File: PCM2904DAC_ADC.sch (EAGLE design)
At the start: 48 parts, among them IC1 LM358D, Q1 12MHz, X1 V+, D-, D+, GND, X2 1503_09, X3 1503_09

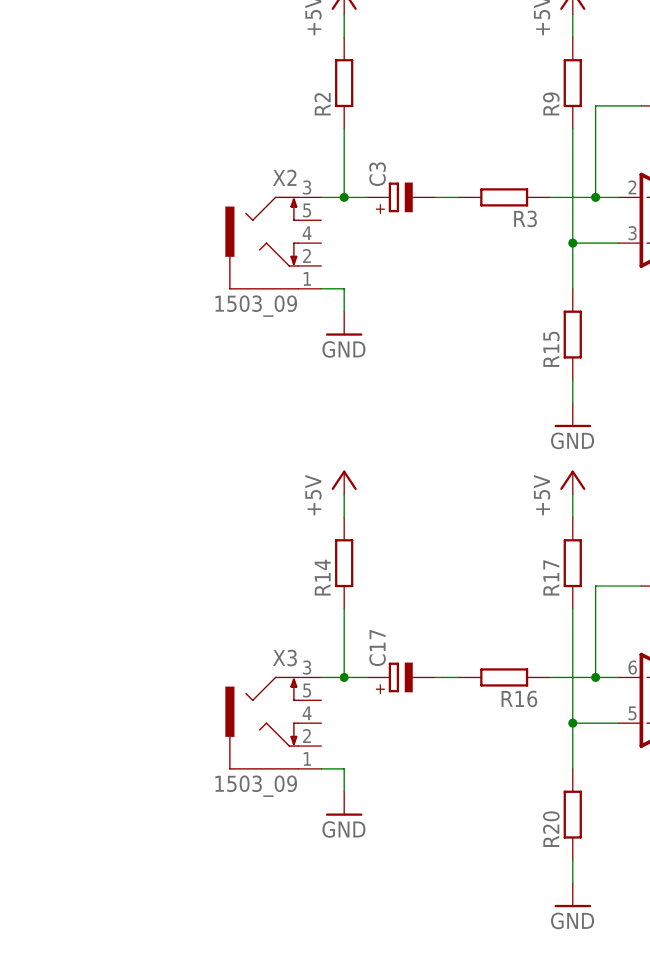
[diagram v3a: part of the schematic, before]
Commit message: cambiado tamaño del led, fichas stereo, y otras cosas sueltas
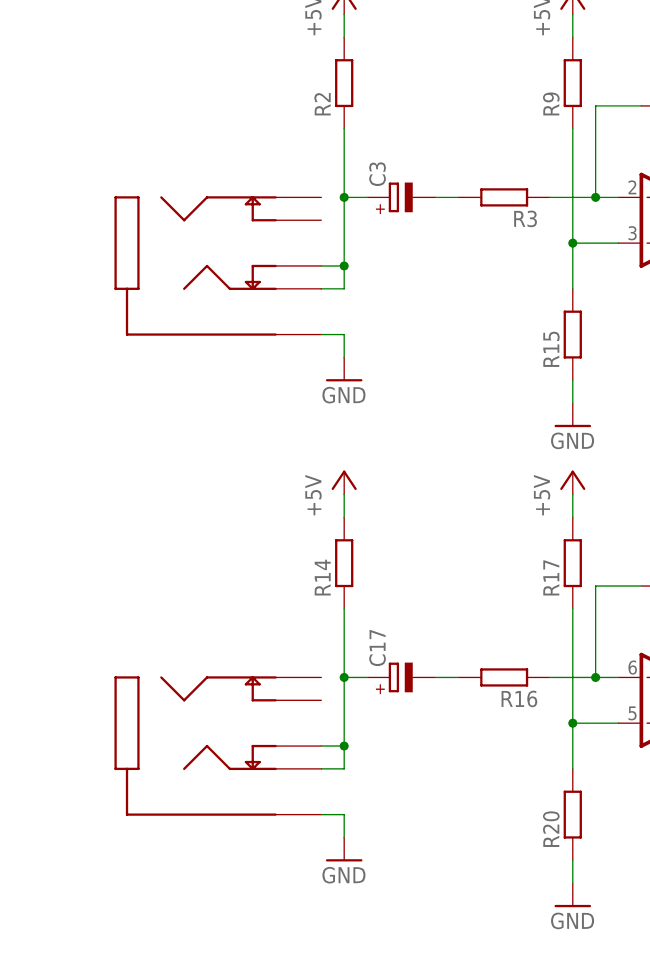
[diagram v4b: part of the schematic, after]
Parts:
- removed X2, X3: 1503_09, con-lumberg:1503_09
- added U$1, U$8: 1/8STEREO, bleep t2:1/8STEREO
- C4: device rcl:CPOL-EU153CLV-0505 -> rcl:CPOL-EU153CLV-0807
- LED1: device led:LEDSML1206 -> led:LEDCHIPLED_0805
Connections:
- net GND: now also U$1.P$1, U$8.P$1; no longer X2.1, X3.1
- net N$5: now also U$8.P$4, U$8.P$5; no longer X2.3
- net N$7: now also U$1.P$4, U$1.P$5; no longer X3.3
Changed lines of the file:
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@@
 <part name="X1" library="con-berg" deviceset="PN61729" device="" value="V+, D-, D+, GND"/>
 <part name="GND2" library="supply1" deviceset="GND" device=""/>
-<part name="C4" library="rcl" deviceset="CPOL-EU" device="153CLV-0505" value="100u "/>
+<part name="C4" library="rcl" library_urn="urn:adsk.eagle:library:334" deviceset="CPOL-EU" device="153CLV-0807" package3d_urn="urn:adsk.eagle:package:23400/1" value="100u "/>
 <part name="R4" library="rcl" deviceset="R-EU_" device="R1206" value="22"/>
 <part name="R5" library="rcl" deviceset="R-EU_" device="R1206" value="22"/>
@@
 <part name="R8" library="rcl" deviceset="R-EU_" device="R1206" value="1k2"/>
 <part name="PCM2904" library="PCM2904" deviceset="PCM2904" device=""/>
-<part name="LED1" library="led" deviceset="LED" device="SML1206" value="2.65V, 2mA"/>
+<part name="LED1" library="led" library_urn="urn:adsk.eagle:library:259" deviceset="LED" device="CHIPLED_0805" package3d_urn="urn:adsk.eagle:package:15821/1" value="2.65V, 2mA"/>
 <part name="IC2" library="bt_regulator" deviceset="LM2931-ADJ" device="M"/>
 <part name="R12" library="rcl" deviceset="R-EU_" device="R1206" value="5k7"/>
 <part name="R13" library="rcl" deviceset="R-EU_" device="R1206" value="10k"/>
-<part name="X2" library="con-lumberg" library_urn="urn:adsk.eagle:library:163" deviceset="1503_09" device="" package3d_urn="urn:adsk.eagle:package:8555/1"/>
 <part name="IC1" library="linear" library_urn="urn:adsk.eagle:library:262" deviceset="LM358" device="D" package3d_urn="urn:adsk.eagle:package:16404/2"/>
 <part name="R2" library="rcl" library_urn="urn:adsk.eagle:library:334" deviceset="R-EU_" device="R1206W" package3d_urn="urn:adsk.eagle:package:23539/1"/>
@@
 <part name="P+6" library="supply1" library_urn="urn:adsk.eagle:library:371" deviceset="+5V" device=""/>
 <part name="C10" library="rcl" library_urn="urn:adsk.eagle:library:334" deviceset="CPOL-EU" device="153CLV-0505" package3d_urn="urn:adsk.eagle:package:23402/1" value="10u"/>
-<part name="X3" library="con-lumberg" library_urn="urn:adsk.eagle:library:163" deviceset="1503_09" device="" package3d_urn="urn:adsk.eagle:package:8555/1"/>
 <part name="R14" library="rcl" library_urn="urn:adsk.eagle:library:334" deviceset="R-EU_" device="R1206W" package3d_urn="urn:adsk.eagle:package:23539/1"/>
 <part name="R16" library="rcl" library_urn="urn:adsk.eagle:library:334" deviceset="R-EU_" device="R1206W" package3d_urn="urn:adsk.eagle:package:23539/1"/>
@@
 <part name="P+9" library="supply1" library_urn="urn:adsk.eagle:library:371" deviceset="+5V" device=""/>
 <part name="GND11" library="supply1" deviceset="GND" device=""/>
+<part name="U$8" library="bleep t2" deviceset="1/8STEREO" device=""/>
+<part name="U$1" library="bleep t2" deviceset="1/8STEREO" device=""/>
 </parts>
 <sheets>
@@
 <instance part="R12" gate="G$1" x="-35.56" y="40.64" rot="R90"/>
 <instance part="R13" gate="G$1" x="-35.56" y="27.94" rot="R270"/>
-<instance part="X2" gate="G$1" x="-86.36" y="-25.4" rot="MR0"/>
 <instance part="IC1" gate="A" x="-40.64" y="-22.86" rot="MR180"/>
 <instance part="R2" gate="G$1" x="-78.74" y="-7.62" rot="R90"/>
@@
 <instance part="P+2" gate="1" x="-78.74" y="2.54"/>
 <instance part="P+3" gate="1" x="-53.34" y="2.54"/>
-<instance part="GND5" gate="1" x="-78.74" y="-35.56"/>
+<instance part="GND5" gate="1" x="-78.74" y="-40.64"/>
 <instance part="GND6" gate="1" x="-53.34" y="-45.72"/>
 <instance part="P+4" gate="1" x="-86.36" y="50.8"/>
@@
 <instance part="P+6" gate="1" x="40.64" y="88.9"/>
 <instance part="C10" gate="G$1" x="-12.7" y="-76.2" rot="R90"/>
-<instance part="X3" gate="G$1" x="-86.36" y="-78.74" rot="MR0"/>
 <instance part="R14" gate="G$1" x="-78.74" y="-60.96" rot="R90"/>
 <instance part="R16" gate="G$1" x="-60.96" y="-73.66" rot="R180"/>
@@
 <instance part="P+7" gate="1" x="-78.74" y="-50.8"/>
 <instance part="P+8" gate="1" x="-53.34" y="-50.8"/>
-<instance part="GND9" gate="1" x="-78.74" y="-88.9"/>
+<instance part="GND9" gate="1" x="-78.74" y="-93.98"/>
 <instance part="GND10" gate="1" x="-53.34" y="-99.06"/>
 <instance part="IC1" gate="B" x="-40.64" y="-76.2" rot="MR180"/>
@@
 <instance part="P+9" gate="1" x="-12.7" y="-30.48"/>
 <instance part="GND11" gate="1" x="-12.7" y="-58.42"/>
+<instance part="U$8" gate="G$1" x="-104.14" y="-25.4" rot="MR180"/>
+<instance part="U$1" gate="G$1" x="-104.14" y="-78.74" rot="MR180"/>
 </instances>
 <busses>
@@
 </segment>
 <segment>
-<pinref part="GND5" gate="1" pin="GND"/>
-<wire x1="-78.74" y1="-33.02" x2="-78.74" y2="-30.48" width="0.1524" layer="91"/>
-<pinref part="X2" gate="G$1" pin="1"/>
-<wire x1="-78.74" y1="-30.48" x2="-81.28" y2="-30.48" width="0.1524" layer="91"/>
-</segment>
-<segment>
 <pinref part="GND6" gate="1" pin="GND"/>
 <pinref part="R15" gate="G$1" pin="1"/>
@@
 <pinref part="GND8" gate="1" pin="GND"/>
 <wire x1="63.5" y1="22.86" x2="63.5" y2="25.4" width="0.1524" layer="91"/>
-</segment>
-<segment>
-<pinref part="GND9" gate="1" pin="GND"/>
-<wire x1="-78.74" y1="-86.36" x2="-78.74" y2="-83.82" width="0.1524" layer="91"/>
-<pinref part="X3" gate="G$1" pin="1"/>
-<wire x1="-78.74" y1="-83.82" x2="-81.28" y2="-83.82" width="0.1524" layer="91"/>
 </segment>
 <segment>
@@
 <junction x="-7.62" y="-53.34"/>
 </segment>
+<segment>
+<pinref part="U$8" gate="G$1" pin="P$1"/>
+<pinref part="GND5" gate="1" pin="GND"/>
+<wire x1="-81.28" y1="-35.56" x2="-78.74" y2="-35.56" width="0.1524" layer="91"/>
+<wire x1="-78.74" y1="-35.56" x2="-78.74" y2="-38.1" width="0.1524" layer="91"/>
+</segment>
+<segment>
+<pinref part="U$1" gate="G$1" pin="P$1"/>
+<pinref part="GND9" gate="1" pin="GND"/>
+<wire x1="-81.28" y1="-88.9" x2="-78.74" y2="-88.9" width="0.1524" layer="91"/>
+<wire x1="-78.74" y1="-88.9" x2="-78.74" y2="-91.44" width="0.1524" layer="91"/>
+</segment>
 </net>
 <net name="N$4" class="0">
@@
 <net name="N$5" class="0">
 <segment>
-<pinref part="X2" gate="G$1" pin="3"/>
 <pinref part="R2" gate="G$1" pin="1"/>
-<wire x1="-81.28" y1="-20.32" x2="-78.74" y2="-20.32" width="0.1524" layer="91"/>
 <wire x1="-78.74" y1="-20.32" x2="-78.74" y2="-12.7" width="0.1524" layer="91"/>
 <pinref part="C3" gate="G$1" pin="+"/>
 <wire x1="-76.2" y1="-20.32" x2="-78.74" y2="-20.32" width="0.1524" layer="91"/>
 <junction x="-78.74" y="-20.32"/>
+<pinref part="U$8" gate="G$1" pin="P$5"/>
+<wire x1="-81.28" y1="-30.48" x2="-78.74" y2="-30.48" width="0.1524" layer="91"/>
+<wire x1="-78.74" y1="-30.48" x2="-78.74" y2="-27.94" width="0.1524" layer="91"/>
+<pinref part="U$8" gate="G$1" pin="P$4"/>
+<wire x1="-78.74" y1="-27.94" x2="-78.74" y2="-20.32" width="0.1524" layer="91"/>
+<wire x1="-81.28" y1="-27.94" x2="-78.74" y2="-27.94" width="0.1524" layer="91"/>
+<junction x="-78.74" y="-27.94"/>
 </segment>
 </net>
@@
 <net name="N$7" class="0">
 <segment>
-<pinref part="X3" gate="G$1" pin="3"/>
 <pinref part="R14" gate="G$1" pin="1"/>
-<wire x1="-81.28" y1="-73.66" x2="-78.74" y2="-73.66" width="0.1524" layer="91"/>
 <wire x1="-78.74" y1="-73.66" x2="-78.74" y2="-66.04" width="0.1524" layer="91"/>
 <pinref part="C17" gate="G$1" pin="+"/>
 <wire x1="-76.2" y1="-73.66" x2="-78.74" y2="-73.66" width="0.1524" layer="91"/>
 <junction x="-78.74" y="-73.66"/>
-</segment>
-</net>
+<pinref part="U$1" gate="G$1" pin="P$5"/>
+<wire x1="-81.28" y1="-83.82" x2="-78.74" y2="-83.82" width="0.1524" layer="91"/>
+<wire x1="-78.74" y1="-83.82" x2="-78.74" y2="-81.28" width="0.1524" layer="91"/>
+<pinref part="U$1" gate="G$1" pin="P$4"/>
+<wire x1="-78.74" y1="-81.28" x2="-78.74" y2="-73.66" width="0.1524" layer="91"/>
+<wire x1="-81.28" y1="-81.28" x2="-78.74" y2="-81.28" width="0.1524" layer="91"/>
+<junction x="-78.74" y="-81.28"/>
+</segment>
+</net>

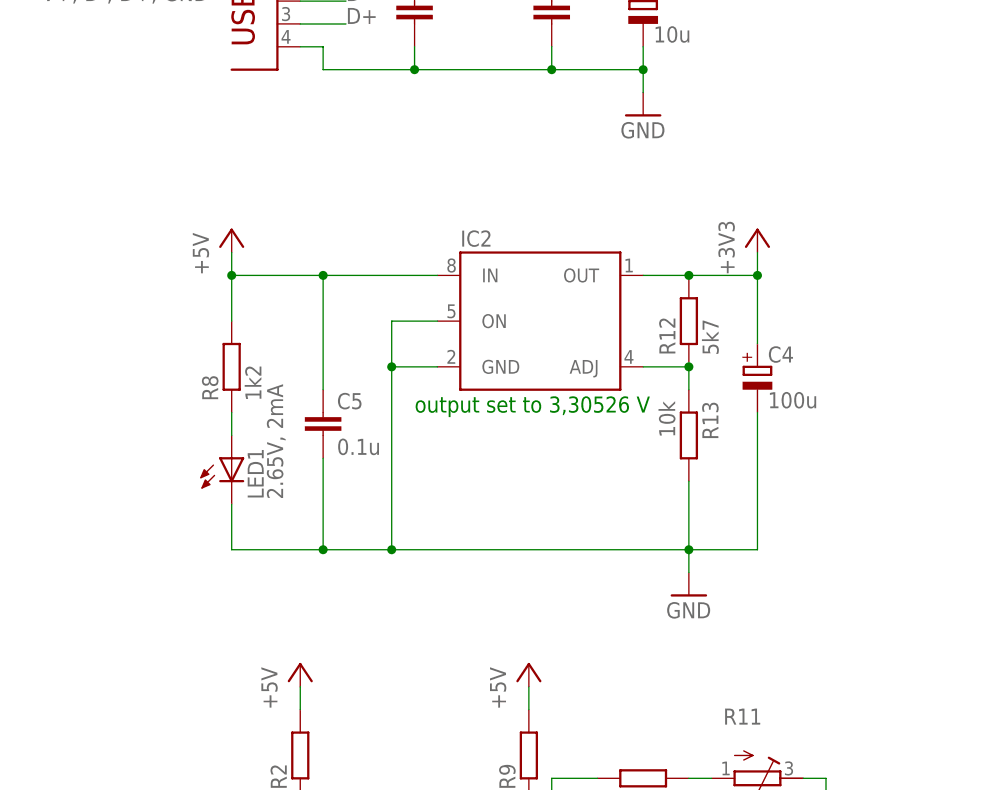
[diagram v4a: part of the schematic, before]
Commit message: Mirror + R 100 Ohms
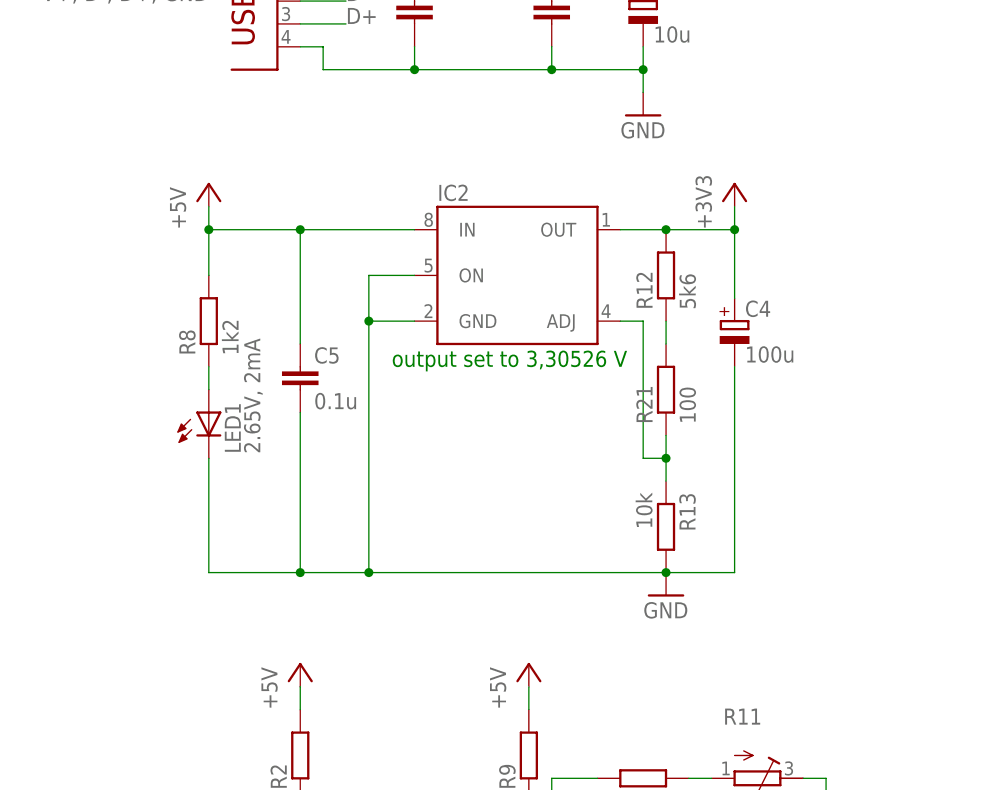
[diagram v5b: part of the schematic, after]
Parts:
- added R21: 100, rcl:R-EU_R1206
- R12: value 5k7 -> 5k6
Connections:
- removed net N$41: IC2.ADJ, R12.1, R13.1
- new net N$26: R12.1, R21.2
- new net N$27: IC2.ADJ, R13.1, R21.1
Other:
- moved on the sheet: C4, C5, IC2, LED1, R12, R13, R8
